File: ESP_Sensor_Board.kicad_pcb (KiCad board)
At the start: 2 copper layers, 38.1 x 38.1 mm, 34 parts, among them J1 USB_B_Micro, Q1 Q_NPN_BEC, Q2 Q_NPN_BEC, Q3 Q_NPN_BEC, U1 LMR62421XMF, U2 ESP32-WROOM-32D, U3 CH340C, U4 LM75B, U5 HP203B, Y1 32.768kHz

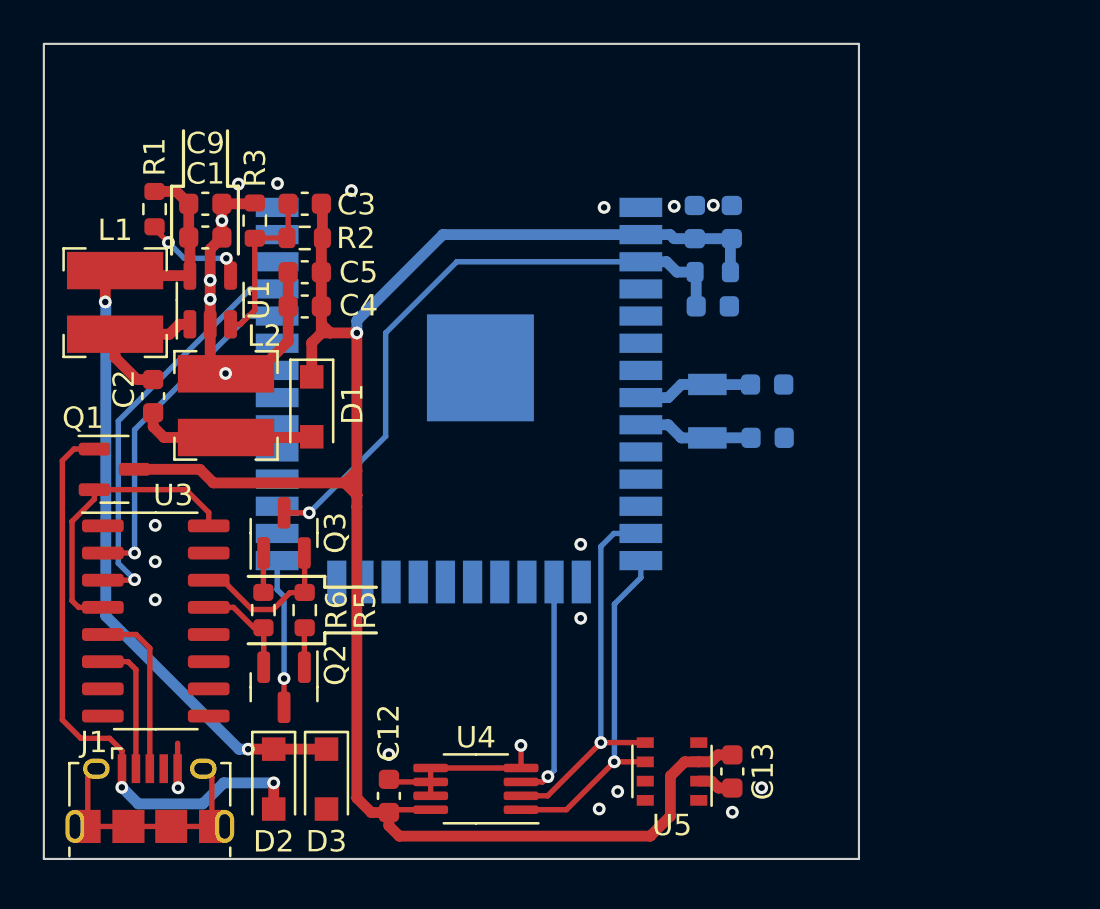
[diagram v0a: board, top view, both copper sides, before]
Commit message: Started work adding voltage divider
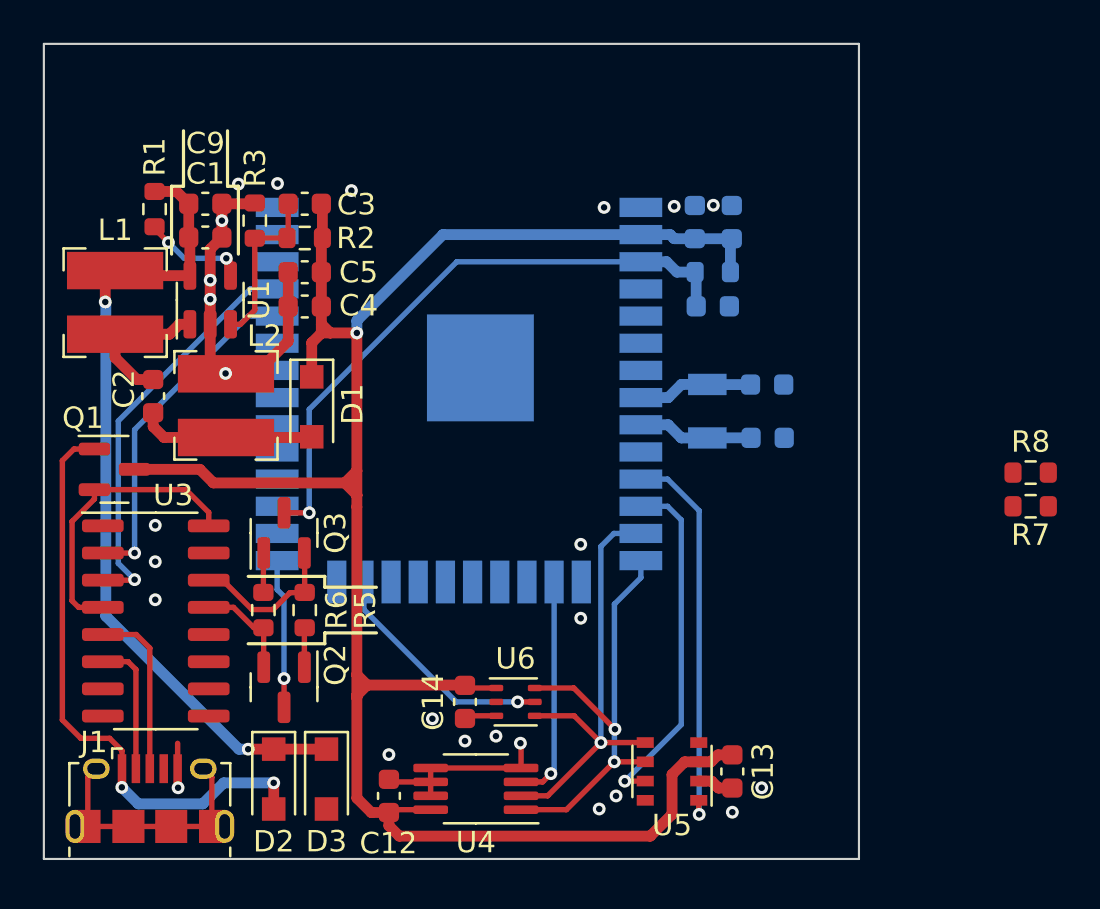
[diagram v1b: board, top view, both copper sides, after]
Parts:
- added C14: 1uF, Capacitor_SMD:C_0603_1608Metric, F.Cu at (83.2, 68.9)
- added R7: 47k, Resistor_SMD:R_0603_1608Metric, F.Cu at (109.6, 59.7)
- added R8: 150k, Resistor_SMD:R_0603_1608Metric, F.Cu at (109.6, 58.1)
- added U6: LTR-303ALS-01, OptoDevice:Lite-On_LTR-303ALS-01, F.Cu at (85.5, 68.9)
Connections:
- U2 pad 11: unconnected-(U2-Pad11) -> /ALT_INT1
- U2 pad 12: unconnected-(U2-Pad12) -> /ALT_INT0
- U2 pad 23: unconnected-(U2-Pad23) -> /LIGHT_INT
- U2 pad 4: unconnected-(U2-Pad4) -> /V_DIV
- U5 pad 1: unconnected-(U5-Pad1) -> /ALT_INT1
- U5 pad 7: unconnected-(U5-Pad7) -> /ALT_INT0
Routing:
- net /ALT_INT1: track 0.00 -> 18.2 mm, vias 0 -> 1
- net /ALT_INT0: track 0.00 -> 16.4 mm, vias 0 -> 1
- net /LIGHT_INT: track 0.00 -> 11.1 mm, vias 0 -> 1
- net /3v3: track 88.8 -> 96.3 mm
- net /I2C1_SDA: track 16.7 -> 21.2 mm, vias 1 -> 2
- net /I2C1_SCL: track 18.1 -> 21.7 mm
- net GND: track 29.2 -> 30.8 mm, vias 22 -> 25

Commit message: Moved sensors to back of board, added battery pads
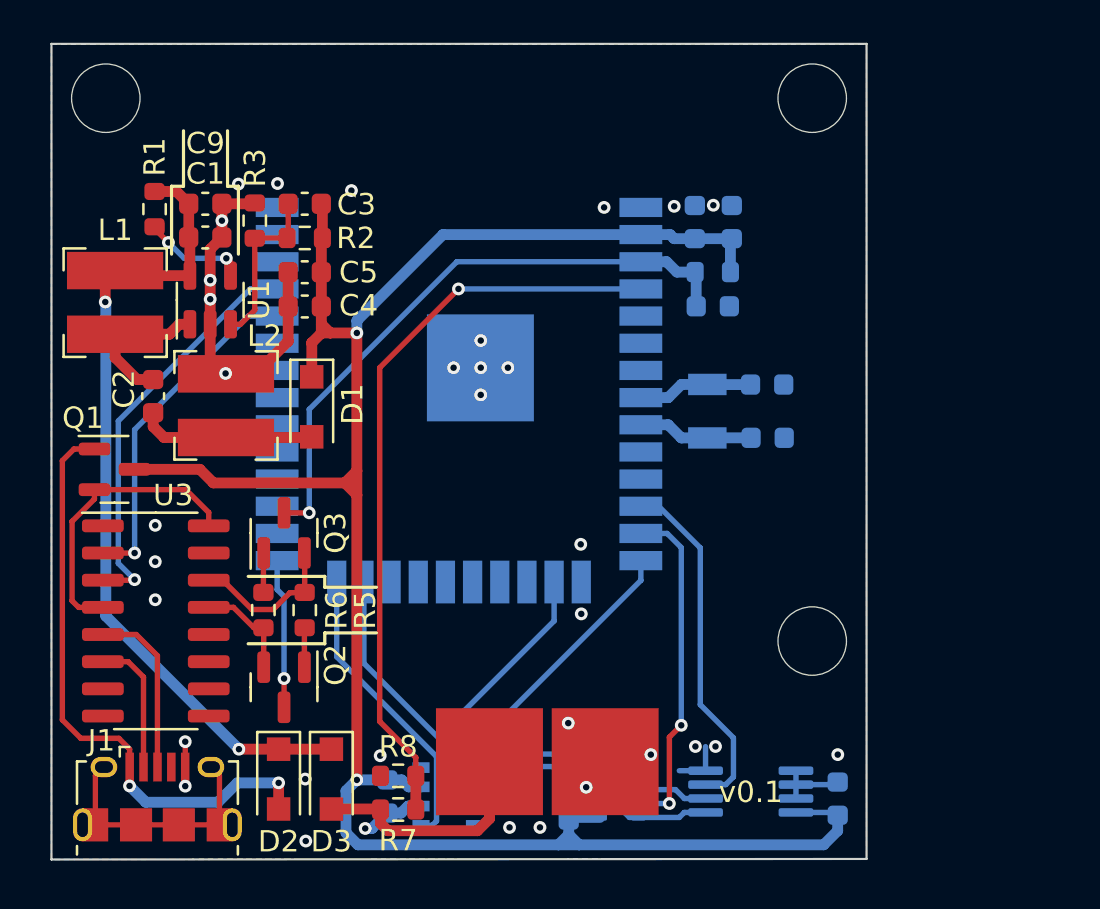
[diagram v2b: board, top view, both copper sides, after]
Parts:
- added H1: MountingHole, MountingHole:MountingHole_3.2mm_M3, F.Cu at (99.4, 66.0)
- added H2: MountingHole, MountingHole:MountingHole_3.2mm_M3, F.Cu at (99.4, 40.6)
- added H3: MountingHole, MountingHole:MountingHole_3.2mm_M3, F.Cu at (66.4, 40.6)
- added U7: Solder_Pad, ESP_Sensor_Board:Pad, F.Cu at (84.3, 71.7)
- added U8: Solder_Pad, ESP_Sensor_Board:Pad, F.Cu at (89.7, 71.7)
- C12, C13, C14, U4, U5, U6: moved to B.Cu
- moved R8 32.8 mm to (80.1, 72.3)
- moved R7 32.8 mm to (80.1, 73.9)
- moved C12 21.0 mm to (100.6, 73.4)
- moved C13 16.2 mm to (79.6, 73.3)
- moved U4 12.8 mm to (96.5, 73.1), turned to 0 degrees
- moved U5 10.6 mm to (82.4, 73.3)
- moved C14 6.79 mm to (88.0, 73.6), turned to 90 degrees
- moved U6 6.79 mm to (90.4, 73.6)
- moved J1 0.36 mm to (68.8, 73.3)
- moved D2 0.23 mm to (74.5, 72.5)
- moved D3 0.23 mm to (76.9, 72.5)
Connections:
- U2 pad 11: /ALT_INT1 -> unconnected-(U2-Pad11)
- U2 pad 12: /ALT_INT0 -> /TEMP_INT
- U2 pad 13: /I2C1_SCL -> /LIGHT_INT
- U2 pad 14: /I2C1_SDA -> /I2C1_SCL
- U2 pad 16: /TEMP_INT -> /I2C1_SDA
- U2 pad 23: /LIGHT_INT -> /ALT_INT0
- U2 pad 24: unconnected-(U2-Pad24) -> /ALT_INT1
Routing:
- net /V_DIV: track 0.00 -> 35.1 mm, vias 0 -> 1
- net /B+: track 0.00 -> 11.1 mm
- net /TEMP_INT: track 10.6 -> 16.4 mm, vias 1 -> 0
- net /LIGHT_INT: track 11.1 -> 15.8 mm, vias 1 -> 2
- net /ALT_INT1: track 18.2 -> 13.9 mm, vias 1 -> 0
- net /I2C1_SDA: track 21.2 -> 25.1 mm, vias 2 -> 0
- net /3v3: track 96.3 -> 100.2 mm, vias 1 -> 2
- net /ALT_INT0: track 16.4 -> 13.0 mm, vias 1 -> 0
- net /I2C1_SCL: track 21.7 -> 25.0 mm, vias 1 -> 0
- net GND: track 30.8 -> 27.6 mm, vias 25 -> 34
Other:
- board text added: "v0.1"
